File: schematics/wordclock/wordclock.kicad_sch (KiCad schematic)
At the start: 14 parts

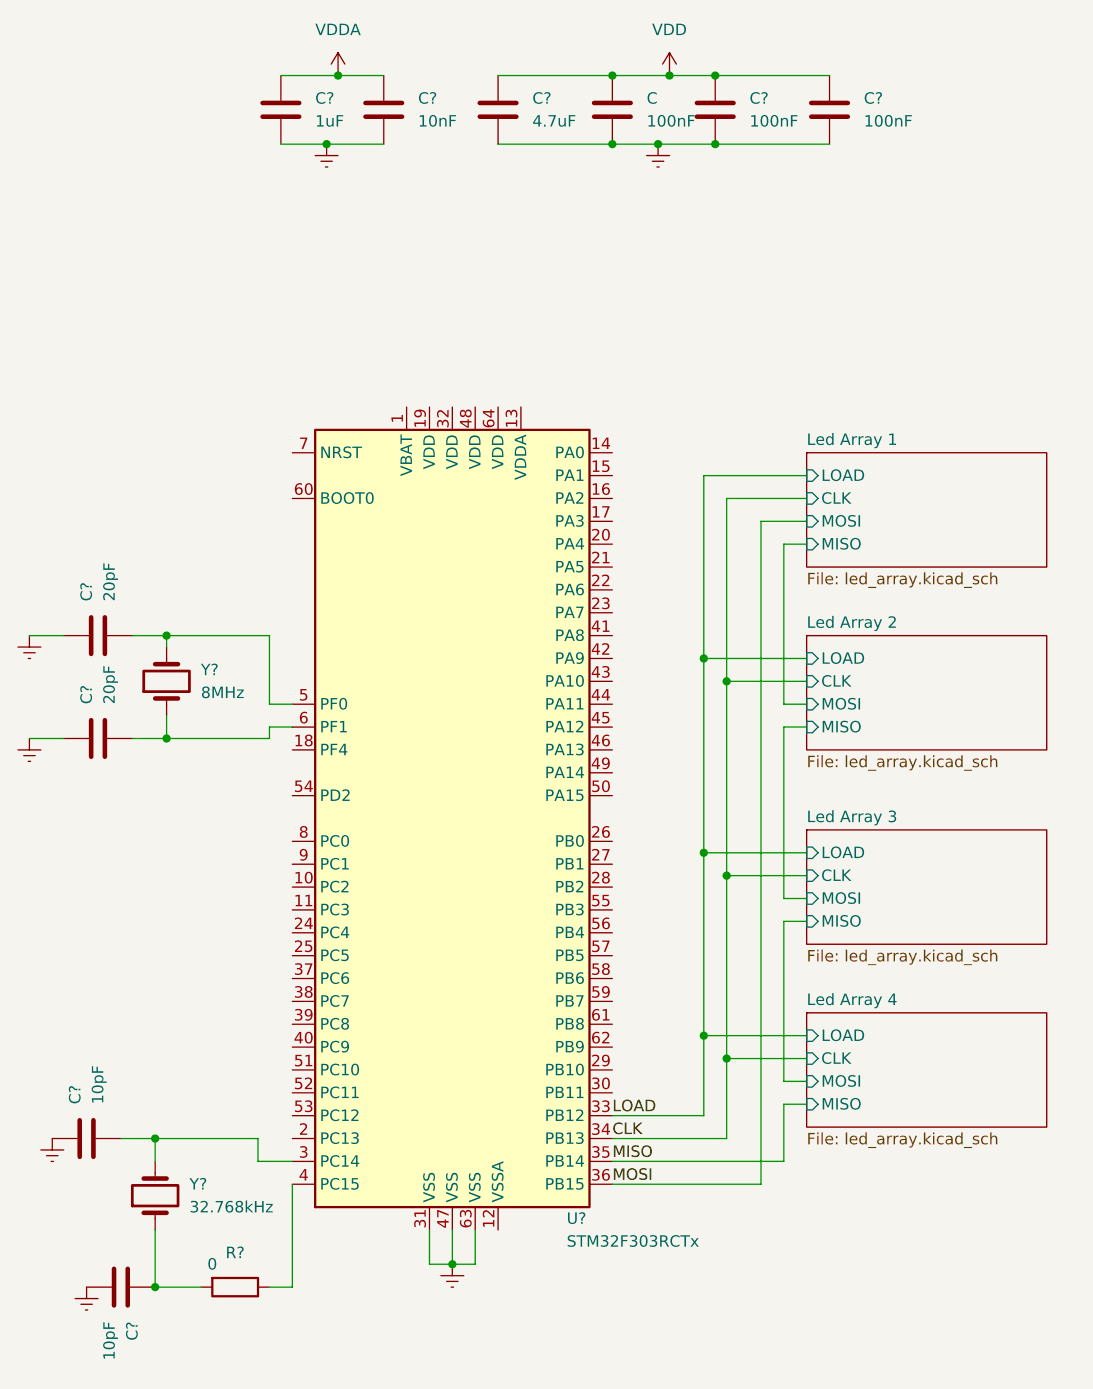
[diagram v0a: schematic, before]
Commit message: Finish defining words, schematic updates
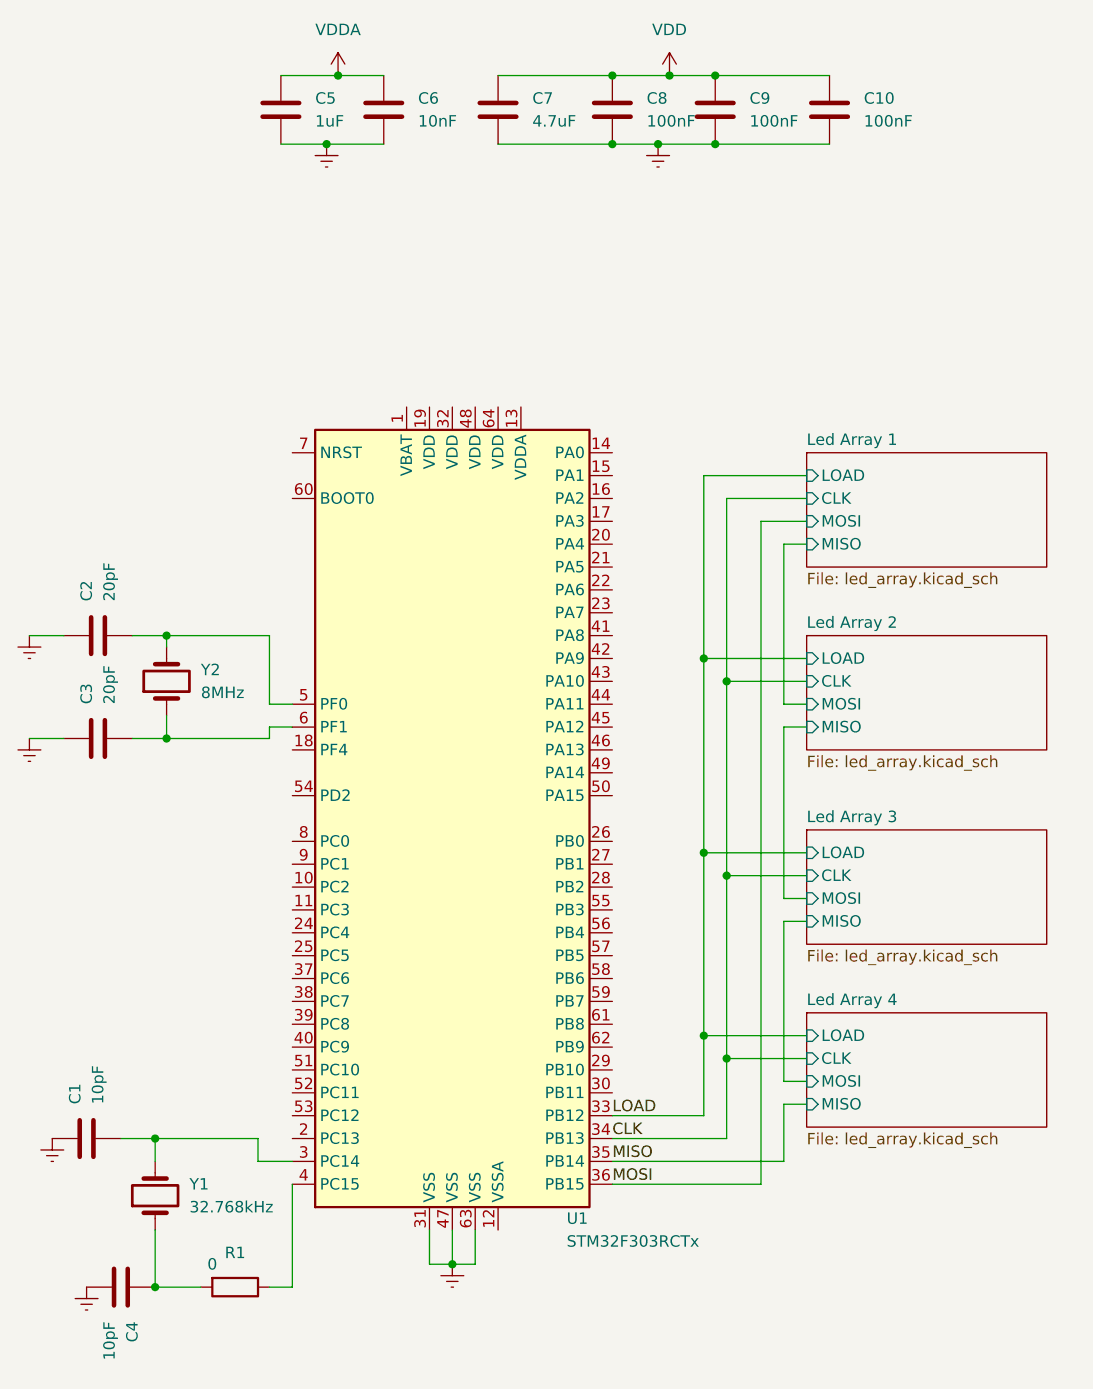
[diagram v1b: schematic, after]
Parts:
- C1, C10, C2, C3, C4, C5, C6, C7, C9: renamed from C?; footprint (none) -> Capacitor_SMD:C_0805_2012Metric
- C8: renamed from C; footprint (none) -> Capacitor_SMD:C_0805_2012Metric
- Y1, Y2: renamed from Y?; footprint (none) -> Crystal:Crystal_SMD_3225-4Pin_3.2x2.5mm
- gave numbers to parts that had none: 2
